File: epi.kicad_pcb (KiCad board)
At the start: 2 copper layers, 12.5 x 23.1 mm, 24 parts, among them J1 Conn_01x12, J2 Conn_01x12, J3 Conn_01x04, J4 USB_C_Receptacle_USB2.0, U1 ATmega32U4-M, Y1 16mhz

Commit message: bit of everything and name change
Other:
- board text added: "10"
- board text added: "12"
- board text added: "14"
- board text added: "15"
- board text added: "16"
- board text added: "2"
- board text added: "4"
- board text added: "5V"
- board text added: "7"
- board text added: "8"
- board text added: "A0"
- board text added: "A1"
- board text added: "A2"
- board text added: "A3"
- board text added: "A4"
- board text added: "A5"
- board text added: "D1"
- board text added: "D2"
- board text added: "GND"
- board text added: "RST"
- board text added: "~11"
- board text added: "~13"
- board text added: "~3"
- board text added: "~5"
- board text added: "~6"
- board text added: "~9"

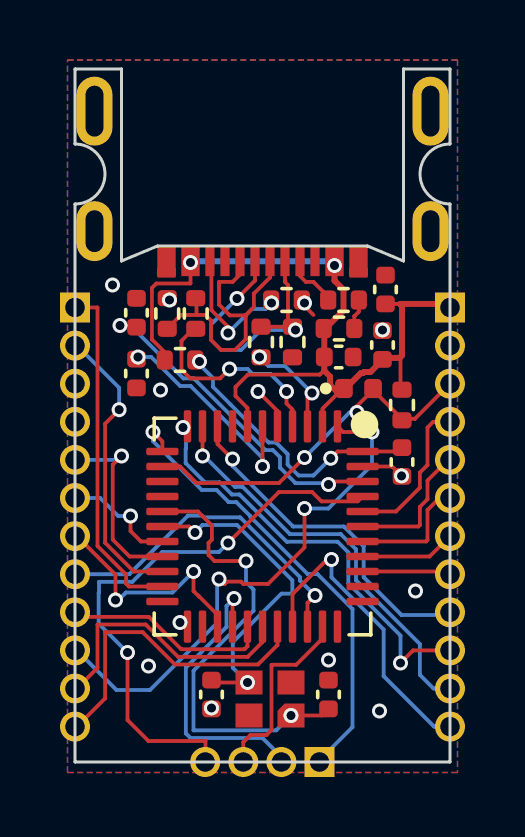
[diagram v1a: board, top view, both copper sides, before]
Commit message: small trace fix
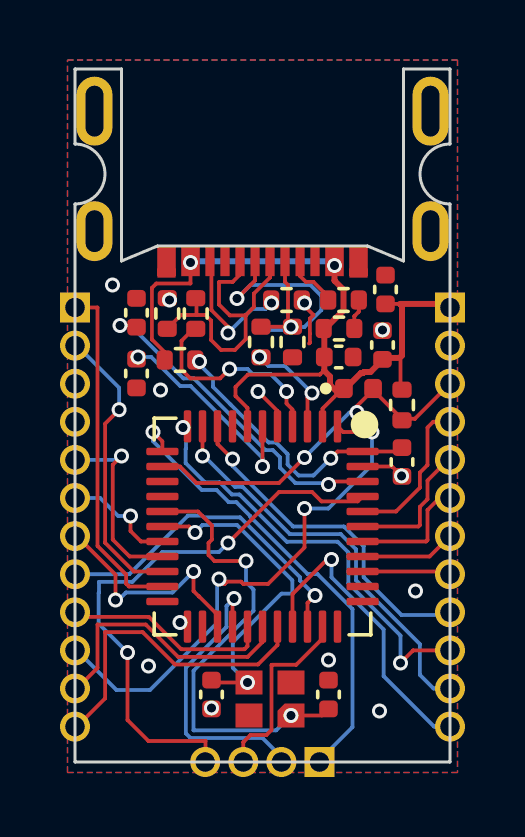
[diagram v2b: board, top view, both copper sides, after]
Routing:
- net GND: track 4.55 -> 5.57 mm
- net Net-(J4-PadA7): track 9.76 -> 10.7 mm
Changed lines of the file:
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@@
   (segment (start 103.06 44.54) (end 103.21 44.39) (width 0.127) (layer "F.Cu") (net 2))
   (segment (start 101.4 44.2) (end 101.7 44.5) (width 0.127) (layer "F.Cu") (net 2))
+  (segment (start 101.5795 45.4205) (end 101.55 45.45) (width 0.127) (layer "F.Cu") (net 2))
   (segment (start 103.3375 49.55) (end 104.32 49.55) (width 0.127) (layer "F.Cu") (net 2))
   (segment (start 104.32 49.55) (end 104.635 49.865) (width 0.127) (layer "F.Cu") (net 2))
   (segment (start 104.635 49.865) (end 104.65 49.88) (width 0.127) (layer "F.Cu") (net 2))
   (segment (start 103.21 44.39) (end 103.21 44) (width 0.127) (layer "F.Cu") (net 2))
+  (segment (start 101.5795 45.1295) (end 101.5795 45.4205) (width 0.127) (layer "F.Cu") (net 2))
   (segment (start 103.06 44.95) (end 103.06 44.54) (width 0.127) (layer "F.Cu") (net 2))
   (segment (start 100.5 47.7) (end 100.5 48.2125) (width 0.127) (layer "F.Cu") (net 2))
@@
   (segment (start 101.4 44.1) (end 101.4 44.2) (width 0.127) (layer "F.Cu") (net 2))
   (segment (start 101.31 44.01) (end 101.31 44) (width 0.127) (layer "F.Cu") (net 2))
+  (segment (start 101.7 44.5) (end 101.5795 44.6205) (width 0.127) (layer "F.Cu") (net 2))
+  (segment (start 101.5795 44.6205) (end 101.5795 45.1295) (width 0.127) (layer "F.Cu") (net 2))
   (via (at 96.2 56.2) (size 0.5) (drill 0.3) (layers "F.Cu" "B.Cu") (free) (net 2))
   (via (at 103.9 57.7) (size 0.5) (drill 0.3) (layers "F.Cu" "B.Cu") (free) (net 2))
@@
   (segment (start 99.2 43.9) (end 99.751169 43.348831) (width 0.127) (layer "F.Cu") (net 16))
   (segment (start 99.95 44.89) (end 101 44.89) (width 0.127) (layer "F.Cu") (net 16))
-  (via (at 101.1 45) (size 0.5) (drill 0.3) (layers "F.Cu" "B.Cu") (net 16))
+  (via (at 100.95 44.9) (size 0.5) (drill 0.3) (layers "F.Cu" "B.Cu") (net 16))
   (via (at 99.15 43.95) (size 0.5) (drill 0.3) (layers "F.Cu" "B.Cu") (net 16))
-  (segment (start 101.1 45) (end 99.95 45) (width 0.127) (layer "B.Cu") (net 16))
-  (segment (start 98.61659 45.6635) (end 98.2865 45.33341) (width 0.127) (layer "B.Cu") (net 16))
-  (segment (start 99.2865 45.6635) (end 98.61659 45.6635) (width 0.127) (layer "B.Cu") (net 16))
-  (segment (start 99.95 45) (end 99.2865 45.6635) (width 0.127) (layer "B.Cu") (net 16))
-  (segment (start 98.2865 44.8135) (end 99.15 43.95) (width 0.127) (layer "B.Cu") (net 16))
-  (segment (start 98.2865 45.33341) (end 98.2865 44.8135) (width 0.127) (layer "B.Cu") (net 16))
+  (segment (start 101.9635 43.86659) (end 101.59691 43.5) (width 0.127) (layer "B.Cu") (net 16))
+  (segment (start 99.6 43.5) (end 99.15 43.95) (width 0.127) (layer "B.Cu") (net 16))
+  (segment (start 101.9635 44.33341) (end 101.9635 43.86659) (width 0.127) (layer "B.Cu") (net 16))
+  (segment (start 101.59691 43.5) (end 99.6 43.5) (width 0.127) (layer "B.Cu") (net 16))
+  (segment (start 100.85 45) (end 99.95 45) (width 0.127) (layer "B.Cu") (net 16))
+  (segment (start 100.95 44.9) (end 101.39691 44.9) (width 0.127) (layer "B.Cu") (net 16))
+  (segment (start 101.39691 44.9) (end 101.9635 44.33341) (width 0.127) (layer "B.Cu") (net 16))
+  (segment (start 100.95 44.9) (end 100.85 45) (width 0.127) (layer "B.Cu") (net 16))
   (segment (start 98.296 44.33679) (end 98.296 42.753189) (width 0.127) (layer "F.Cu") (net 18))
   (segment (start 98.85 45.1) (end 98.85 44.89079) (width 0.127) (layer "F.Cu") (net 18))
